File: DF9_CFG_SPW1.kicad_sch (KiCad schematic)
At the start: 11 parts, among them J1 Picoblade_CFG, J2 DF9-41P-1V32, J3 DF9-CFG-SPW1, U7 TPS3828-33DBVR

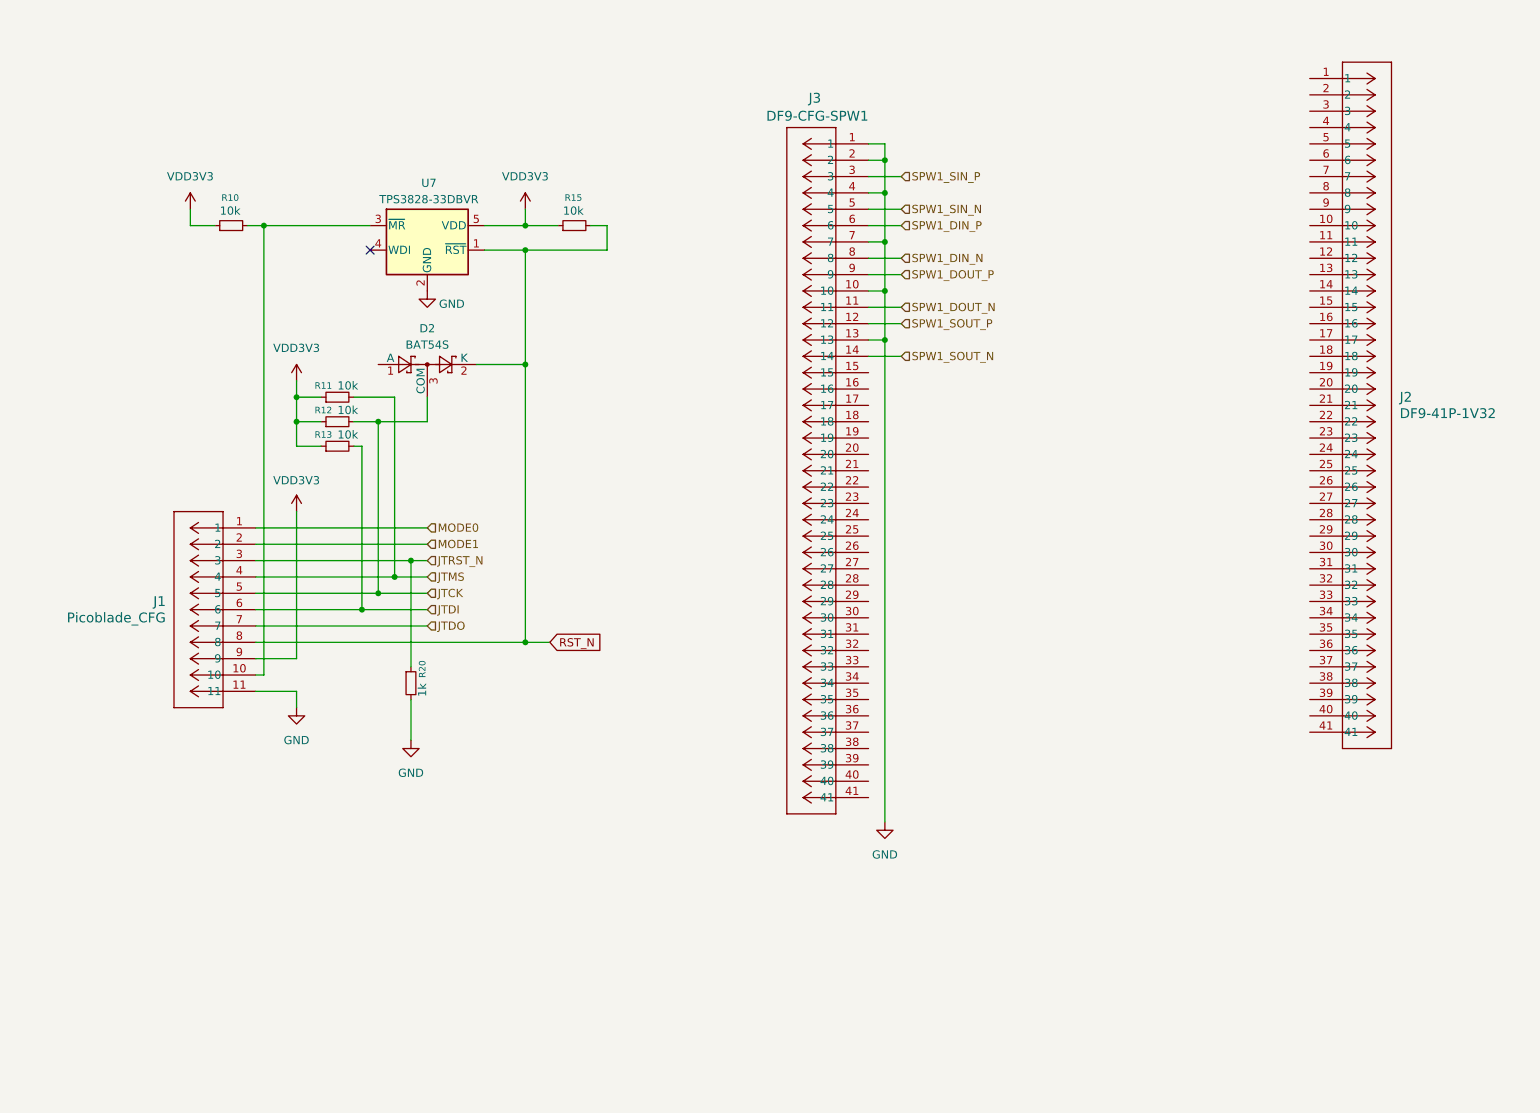
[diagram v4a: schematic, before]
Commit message: CFG, bga sdram, banks to connectors, docoupling
Finished completely routing bga sdram, finished tracing Banks to connectors DF9. Finished tracing Picoblade, diode, reset supervisor. Finished tracing LEDS on bank 5. Finished decoupling all banks and core. Missing only the power tree and power rail level decoupling.
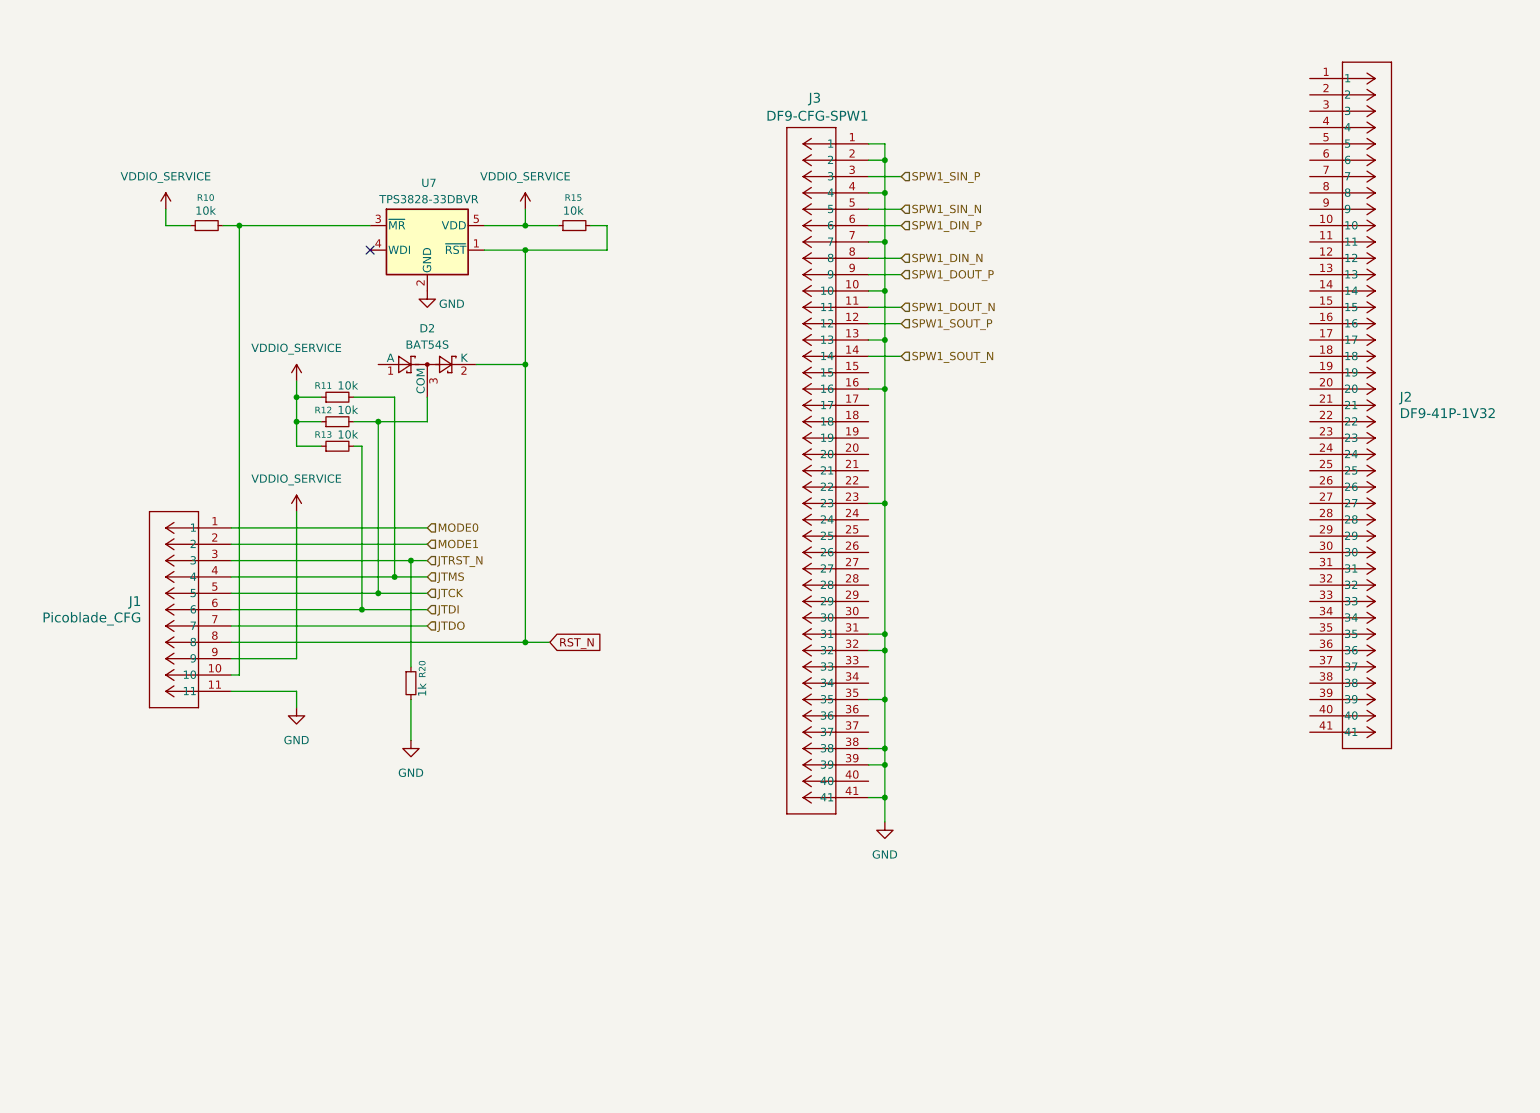
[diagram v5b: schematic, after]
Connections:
- net GND: now also J3.16, J3.23, J3.31, J3.32, J3.35, J3.38, J3.39, J3.41
- net VDD3V3 renamed VDDIO_SERVICE
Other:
- moved on the sheet: J1, R10

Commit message: power tree
power tree defined. Few changes remaining but almost finalized
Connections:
- net GND: now also J2.10, J2.12, J2.13, J2.15, J2.17, J2.18, J2.20, J2.22, J2.24, J2.29
- net B0_11P_DF9: now reaches J3.15
- net B0_09N_DF9: now reaches J3.17
- net B0_06P_DF9: now reaches J3.18
- net B0_05P_DF9: now reaches J3.19
- net B0_07P_DF9: now reaches J3.20
- net B0_01N_DF9: now reaches J3.21
- net B0_08P_DF9: now reaches J3.22
- net B0_03P_DF9: now reaches J3.24
- net B0_09P_DF9: now reaches J3.25
- net B0_03N_DF9: now reaches J3.26
- net B0_06N_DF9: now reaches J3.27
- net B0_10N_DF9: now reaches J3.28
- net B0_01P_DF9: now reaches J3.29
- net B0_02P_DF9: now reaches J3.30
- net B0_07N_DF9: now reaches J3.33
- net B0_02N_DF9: now reaches J3.34
- net B0_04N_DF9: now reaches J3.36
- net B0_10P_DF9: now reaches J3.37
- net B0_04P_DF9: now reaches J3.40
- net +1V7_IN: now reaches J2.1
- net +1V7_IN: now also J2.11, J2.3, J2.5, J2.7, J2.9
- net +5V_IN: now reaches J2.14
- net +5V_IN: now also J2.16
- net +3V3_IN: now reaches J2.19
- net +3V3_IN: now also J2.21, J2.23, J2.25, J2.27
- net +3V6_IN: now reaches J2.2
- net +3V6_IN: now also J2.4, J2.6, J2.8
- net B5_12N_DF9: now reaches J2.26
- net B5_12P_DF9: now reaches J2.28
- net B5_11N_DF9: now reaches J2.30
- net B5_13N_DF9: now reaches J2.31
- net B5_11P_DF9: now reaches J2.32
- net B5_10N_DF9: now reaches J2.33
- net B5_08N_DF9: now reaches J2.34
- net B5_10P_DF9: now reaches J2.35
- net B5_08P_DF9: now reaches J2.36
- net B5_07N_DF9: now reaches J2.37
- net B5_03N_DF9: now reaches J2.38
- net B5_04N_DF9: now reaches J2.39
- net B5_03P_DF9: now reaches J2.40
- net B5_09N_DF9: now reaches J2.41

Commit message: finished
power planes, decoupling, ERC, DRC
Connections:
- no-connect marks 1 -> 2
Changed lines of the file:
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@@
+	)
+	(no_connect
+		(at 76.2 78.74)
 	)
 	(no_connect
